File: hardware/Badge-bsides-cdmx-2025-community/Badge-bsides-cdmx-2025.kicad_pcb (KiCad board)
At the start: 2 copper layers, 49.9 x 109.8 mm, 51 parts, among them J1 SWDIO, J3 ADDON, J4 Conn_01x04_Pin, J5 I2C, J6 Conn_01x04_Pin, P6 USB_C_Plug_USB2.0, Q3 DMG3415U-7, SW10 SW_Push, SW11 ON, SW2 RESET, SW7 SW_Push, SW8 SW_Push, SW9 SW_Push, U1 PY32F030F28U6TR, U6 AP2112K-3.3

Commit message: feat(Hw):Update_BOM_And_Route
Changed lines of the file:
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@@
 				(font
 					(size 0.001 0.001)
+					(thickness 0.15)
 				)
 			)
@@
 				(font
 					(size 0.001 0.001)
+					(thickness 0.15)
 				)
 			)
@@
 				(font
 					(size 0.001 0.001)
+					(thickness 0.15)
 				)
 			)
@@
 				(font
 					(size 0.001 0.001)
+					(thickness 0.15)
 				)
 			)
@@
 				(font
 					(size 0.001 0.001)
+					(thickness 0.15)
 				)
 				(justify mirror)
@@
 				(font
 					(size 0.001 0.001)
+					(thickness 0.15)
 				)
 				(justify mirror)
@@
 				(font
 					(size 0.001 0.001)
+					(thickness 0.15)
 				)
 				(justify mirror)
@@
 				(font
 					(size 0.001 0.001)
+					(thickness 0.15)
 				)
 				(justify mirror)
@@
 				(font
 					(size 0.001 0.001)
+					(thickness 0.15)
 				)
 				(justify mirror)
@@
 				(font
 					(size 0.001 0.001)
+					(thickness 0.15)
 				)
 				(justify mirror)
@@
 				(font
 					(size 0.001 0.001)
+					(thickness 0.15)
 				)
 				(justify mirror)
@@
 				(font
 					(size 0.001 0.001)
+					(thickness 0.15)
 				)
 				(justify mirror)
@@
 				(font
 					(size 0.001 0.001)
+					(thickness 0.15)
 				)
 				(justify mirror)
@@
 				(font
 					(size 0.001 0.001)
+					(thickness 0.15)
 				)
 				(justify mirror)
@@
 				(font
 					(size 0.001 0.001)
+					(thickness 0.15)
 				)
 				(justify mirror)
@@
 				(font
 					(size 0.001 0.001)
+					(thickness 0.15)
 				)
 				(justify mirror)
@@
 	)
 	(segment
-		(start 64.281333 83.964333)
-		(end 61.731333 83.964333)
-		(width 0.3)
-		(layer "F.Cu")
-		(net 2)
-	)
-	(segment
-		(start 64.891333 79.654333)
-		(end 64.891333 83.354333)
+		(start 65.921333 64.844333)
+		(end 65.921333 79.314333)
 		(width 0.3)
 		(layer "F.Cu")
@@
 	)
 	(segment
-		(start 64.891333 83.354333)
-		(end 64.281333 83.964333)
+		(start 36.341333 49.754333)
+		(end 37.341333 50.754333)
 		(width 0.3)
 		(layer "F.Cu")
@@
 	)
 	(segment
-		(start 65.921333 64.844333)
-		(end 65.921333 79.314333)
+		(start 73.891333 58.334333)
+		(end 73.891333 62.694333)
 		(width 0.3)
 		(layer "F.Cu")
@@
 	)
 	(segment
-		(start 36.341333 49.754333)
-		(end 37.341333 50.754333)
+		(start 63.995 87.305)
+		(end 64.891333 86.408667)
 		(width 0.3)
 		(layer "F.Cu")
@@
 	)
 	(segment
-		(start 73.891333 58.334333)
-		(end 73.891333 62.694333)
+		(start 64.891333 86.408667)
+		(end 64.891333 79.654333)
 		(width 0.3)
 		(layer "F.Cu")
@@
 	)
 	(via
-		(at 61.731333 83.964333)
+		(at 63.995 87.305)
 		(size 0.6)
 		(drill 0.3)
@@
 	)
 	(segment
-		(start 61.65 84.045666)
-		(end 61.731333 83.964333)
-		(width 0.3)
-		(layer "B.Cu")
-		(net 2)
-	)
-	(segment
 		(start 43.76 50.754333)
 		(end 41.081333 50.754333)
@@
 	)
 	(segment
-		(start 61.35 88.22)
-		(end 61.65 87.92)
-		(width 0.3)
-		(layer "B.Cu")
-		(net 2)
-	)
-	(segment
 		(start 53.875 63.348)
 		(end 53.88 63.343)
@@
 	)
 	(segment
-		(start 61.65 87.92)
-		(end 61.65 84.045666)
+		(start 63.995 87.305)
+		(end 63.08 88.22)
 		(width 0.3)
 		(layer "B.Cu")
@@
 	)
 	(segment
+		(start 63.08 88.22)
+		(end 51.01 88.22)
+		(width 0.3)
+		(layer "B.Cu")
+		(net 2)
+	)
+	(segment
 		(start 51 88.22)
 		(end 51.01 88.22)
@@
 	)
 	(segment
-		(start 51.01 88.22)
-		(end 61.35 88.22)
-		(width 0.3)
-		(layer "B.Cu")
-		(net 2)
-	)
-	(segment
 		(start 43.76 50.754333)
 		(end 43.885666 50.754333)
@@
 	)
 	(segment
-		(start 46.94 65.42)
-		(end 45.6 64.08)
+		(start 45.6 33.85)
+		(end 45.21 33.46)
 		(width 0.2)
 		(layer "F.Cu")
@@
 	)
 	(segment
-		(start 51.962333 66.012333)
-		(end 51.37 65.42)
+		(start 46.94 65.42)
+		(end 45.6 64.08)
 		(width 0.2)
 		(layer "F.Cu")
@@
 	)
 	(segment
-		(start 51.962333 78.067667)
-		(end 51.962333 66.012333)
+		(start 51.96 78.07)
+		(end 51.962333 78.067667)
 		(width 0.2)
 		(layer "F.Cu")
@@
 	)
 	(segment
-		(start 51.96 78.07)
-		(end 51.962333 78.067667)
+		(start 45.6 64.08)
+		(end 45.6 33.85)
 		(width 0.2)
 		(layer "F.Cu")
@@
 	)
 	(segment
-		(start 45.6 33.56)
-		(end 45.5 33.46)
+		(start 45.21 33.46)
+		(end 42.93125 33.46)
 		(width 0.2)
 		(layer "F.Cu")
@@
 	)
 	(segment
-		(start 45.5 33.46)
-		(end 42.93125 33.46)
+		(start 51.962333 66.012333)
+		(end 51.37 65.42)
 		(width 0.2)
 		(layer "F.Cu")
@@
 	)
 	(segment
-		(start 45.6 64.08)
-		(end 45.6 33.56)
+		(start 51.962333 78.067667)
+		(end 51.962333 66.012333)
 		(width 0.2)
 		(layer "F.Cu")
@@
 	)
 	(segment
-		(start 81.59 109.73569)
-		(end 81.59 108.853)
-		(width 0.5)
-		(layer "B.Cu")
-		(net 26)
-	)
-	(segment
 		(start 82.014848 112.489502)
-		(end 82.014848 110.160538)
+		(end 82.014848 109.277848)
 		(width 0.5)
 		(layer "B.Cu")
@@
 	)
 	(segment
-		(start 44.25 107.344333)
-		(end 43.04 106.134333)
-		(width 0.5)
-		(layer "B.Cu")
-		(net 26)
-	)
-	(segment
-		(start 82.014848 110.160538)
-		(end 81.59 109.73569)
+		(start 82.014848 109.277848)
+		(end 80.081333 107.344333)
 		(width 0.5)
 		(layer "B.Cu")
@@
 	)
 	(segment
-		(start 81.59 108.853)
-		(end 80.081333 107.344333)
+		(start 44.25 107.344333)
+		(end 43.04 106.134333)
 		(width 0.5)
 		(layer "B.Cu")

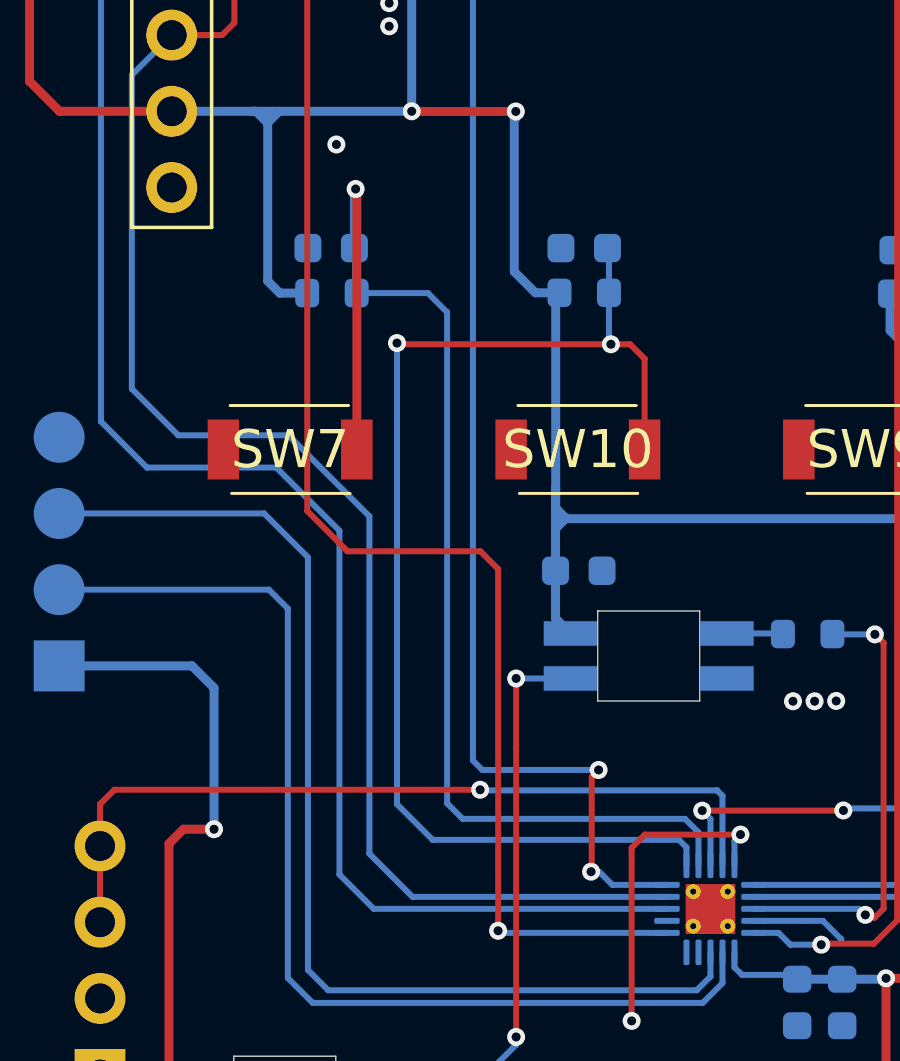
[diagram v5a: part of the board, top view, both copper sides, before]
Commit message: feat(Hw):BoM_Updated_Staff_Community
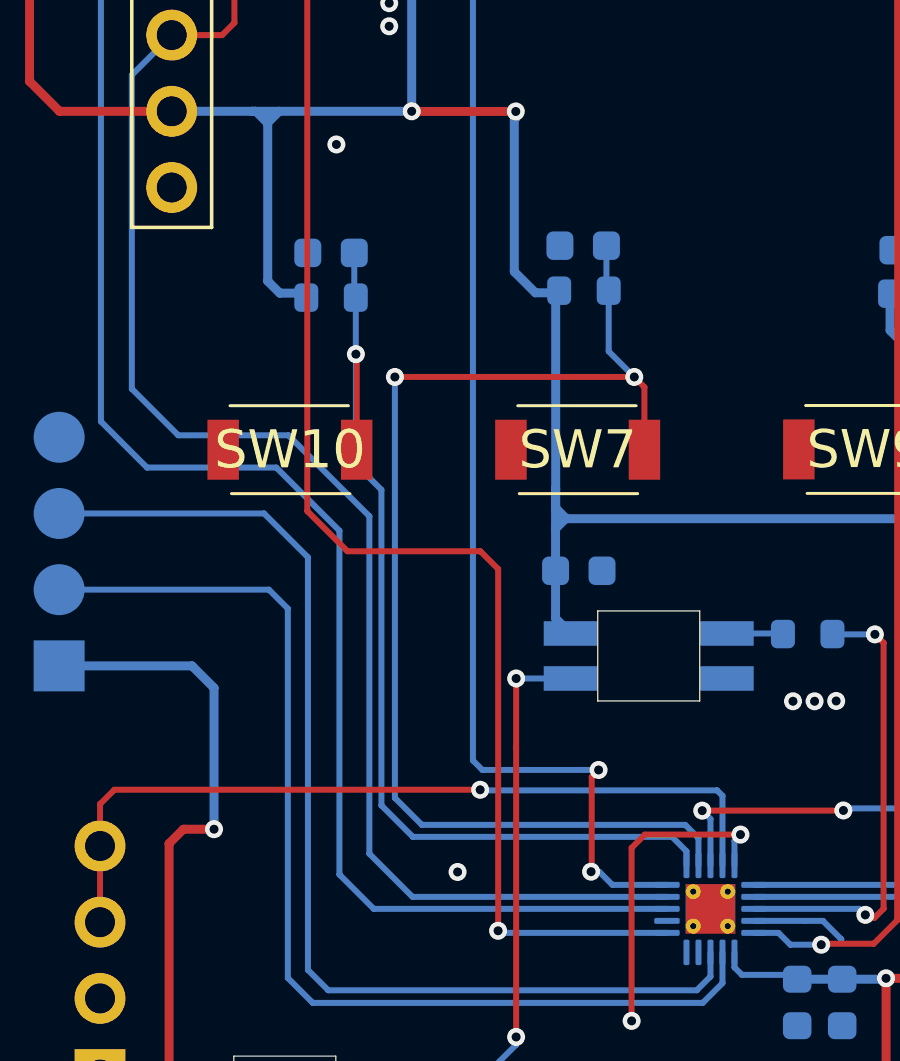
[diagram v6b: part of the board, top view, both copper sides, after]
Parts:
- moved SW10 9.60 mm to (45.0, 62.0)
- moved SW7 9.59 mm to (54.6, 62.0)
- moved C70 8.44 mm to (46.4, 55.5)
- moved R8 8.44 mm to (46.4, 57.0)
- moved R7 8.40 mm to (54.8, 56.7)
- moved C69 8.40 mm to (54.8, 55.2)
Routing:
- net /BTTN4: track 41.0 -> 33.3 mm, vias 2 -> 1
- net /BTTN3: track 41.7 -> 40.9 mm, vias 1 -> 2
- net GND: vias 7 -> 8
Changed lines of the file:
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@@
 	(footprint "Footprints:TS1088R02026"
 		(layer "F.Cu")
-		(at 54.618 62.026595)
+		(at 45.022 62.033405)
 		(descr "TS-1088R-02026-1")
 		(tags "Switch")
@@
 	(footprint "Footprints:TS1088R02026"
 		(layer "F.Cu")
-		(at 45.026333 62.026595)
+		(at 54.613667 62.033405)
 		(descr "TS-1088R-02026-1")
 		(tags "Switch")
@@
 	(footprint "Capacitor_SMD:C_0603_1608Metric"
 		(layer "B.Cu")
-		(at 46.396333 55.314333 180)
+		(at 54.796333 55.234333 180)
 		(descr "Capacitor SMD 0603 (1608 Metric), square (rectangular) end terminal, IPC-7351 nominal, (Body size source: IPC-SM-782 page 76, https://www.pcb-3d.com/wordpress/wp-content/uploads/ipc-sm-782a_amendment_1_and_2.pdf), generated with kicad-footprint-generator")
 		(tags "capacitor")
@@
 	(footprint "Resistor_SMD:R_0603_1608Metric"
 		(layer "B.Cu")
-		(at 46.421333 56.814333 180)
+		(at 54.821333 56.734333 180)
 		(descr "Resistor SMD 0603 (1608 Metric), square (rectangular) end terminal, IPC-7351 nominal, (Body size source: IPC-SM-782 page 72, https://www.pcb-3d.com/wordpress/wp-content/uploads/ipc-sm-782a_amendment_1_and_2.pdf), generated with kicad-footprint-generator")
 		(tags "resistor")
@@
 	(footprint "Resistor_SMD:R_0603_1608Metric"
 		(layer "B.Cu")
-		(at 54.831333 56.804333 180)
+		(at 46.391333 56.964333 180)
 		(descr "Resistor SMD 0603 (1608 Metric), square (rectangular) end terminal, IPC-7351 nominal, (Body size source: IPC-SM-782 page 72, https://www.pcb-3d.com/wordpress/wp-content/uploads/ipc-sm-782a_amendment_1_and_2.pdf), generated with kicad-footprint-generator")
 		(tags "resistor")
@@
 	(footprint "Capacitor_SMD:C_0603_1608Metric"
 		(layer "B.Cu")
-		(at 54.831333 55.314333 180)
+		(at 46.391333 55.474333 180)
 		(descr "Capacitor SMD 0603 (1608 Metric), square (rectangular) end terminal, IPC-7351 nominal, (Body size source: IPC-SM-782 page 76, https://www.pcb-3d.com/wordpress/wp-content/uploads/ipc-sm-782a_amendment_1_and_2.pdf), generated with kicad-footprint-generator")
 		(tags "capacitor")
@@
 	)
 	(via
+		(at 50.61 76.11)
+		(size 0.6)
+		(drill 0.3)
+		(layers "F.Cu" "B.Cu")
+		(free yes)
+		(net 1)
+	)
+	(via
 		(at 46.57 51.86)
 		(size 0.6)
@@
 	)
 	(segment
-		(start 47.211333 53.344333)
-		(end 47.251333 53.384333)
-		(width 0.3)
+		(start 56.838667 59.948667)
+		(end 56.838667 62.033405)
+		(width 0.2)
 		(layer "F.Cu")
 		(net 31)
 	)
 	(segment
-		(start 47.251333 53.384333)
-		(end 47.251333 62.026595)
-		(width 0.3)
+		(start 56.5 59.61)
+		(end 48.52 59.61)
+		(width 0.2)
+		(layer "F.Cu")
+		(net 31)
+	)
+	(segment
+		(start 56.5 59.61)
+		(end 56.838667 59.948667)
+		(width 0.2)
 		(layer "F.Cu")
 		(net 31)
 	)
 	(via
-		(at 47.211333 53.344333)
+		(at 56.5 59.61)
 		(size 0.6)
 		(drill 0.3)
@@
 		(net 31)
 	)
-	(segment
-		(start 58.64 75.89)
-		(end 58.64 74.79)
-		(width 0.2)
-		(layer "B.Cu")
+	(via
+		(at 48.52 59.61)
+		(size 0.6)
+		(drill 0.3)
+		(layers "F.Cu" "B.Cu")
 		(net 31)
 	)
 	(segment
-		(start 58.19 74.34)
-		(end 50.78 74.34)
+		(start 55.571333 55.234333)
+		(end 55.571333 56.659333)
 		(width 0.2)
 		(layer "B.Cu")
@@
 	)
 	(segment
-		(start 47.246333 55.389333)
-		(end 47.171333 55.314333)
-		(width 0.3)
-		(layer "B.Cu")
-		(net 31)
-	)
-	(segment
-		(start 50.261333 73.821333)
-		(end 50.261333 57.454333)
+		(start 58.64 75.89)
+		(end 58.64 74.98)
 		(width 0.2)
 		(layer "B.Cu")
@@
 	)
 	(segment
-		(start 47.246333 56.814333)
-		(end 47.246333 55.389333)
-		(width 0.3)
+		(start 58.64 74.98)
+		(end 58.2 74.54)
+		(width 0.2)
 		(layer "B.Cu")
 		(net 31)
 	)
 	(segment
-		(start 50.261333 57.454333)
-		(end 49.621333 56.814333)
+		(start 58.2 74.54)
+		(end 49.42 74.54)
 		(width 0.2)
 		(layer "B.Cu")
@@
 	)
 	(segment
-		(start 50.78 74.34)
-		(end 50.261333 73.821333)
+		(start 49.42 74.54)
+		(end 48.52 73.64)
 		(width 0.2)
 		(layer "B.Cu")
@@
 	)
 	(segment
-		(start 49.621333 56.814333)
-		(end 47.246333 56.814333)
+		(start 48.52 73.64)
+		(end 48.52 59.61)
 		(width 0.2)
 		(layer "B.Cu")
@@
 	)
 	(segment
-		(start 47.171333 53.384333)
-		(end 47.211333 53.344333)
-		(width 0.3)
+		(start 55.646333 56.734333)
+		(end 55.646333 58.756333)
+		(width 0.2)
 		(layer "B.Cu")
 		(net 31)
 	)
 	(segment
-		(start 47.171333 55.314333)
-		(end 47.171333 53.384333)
-		(width 0.3)
+		(start 55.646333 58.756333)
+		(end 56.5 59.61)
+		(width 0.2)
 		(layer "B.Cu")
 		(net 31)
 	)
 	(segment
-		(start 58.64 74.79)
-		(end 58.19 74.34)
+		(start 55.571333 56.659333)
+		(end 55.646333 56.734333)
 		(width 0.2)
 		(layer "B.Cu")
@@
 	)
 	(segment
-		(start 48.59 58.48)
-		(end 48.63 58.52)
+		(start 47.247 58.877)
+		(end 47.247 62.033405)
 		(width 0.2)
 		(layer "F.Cu")
@@
 	)
 	(segment
-		(start 48.63 58.52)
-		(end 55.72 58.52)
-		(width 0.2)
-		(layer "F.Cu")
-		(net 32)
-	)
-	(segment
-		(start 56.843 59.003)
-		(end 56.36 58.52)
-		(width 0.2)
-		(layer "F.Cu")
-		(net 32)
-	)
-	(segment
-		(start 56.36 58.52)
-		(end 55.72 58.52)
-		(width 0.2)
-		(layer "F.Cu")
-		(net 32)
-	)
-	(segment
-		(start 56.843 62.026595)
-		(end 56.843 59.003)
+		(start 47.22 58.85)
+		(end 47.247 58.877)
 		(width 0.2)
 		(layer "F.Cu")
@@
 	)
 	(via
-		(at 55.72 58.52)
+		(at 47.22 58.85)
 		(size 0.6)
 		(drill 0.3)
@@
 		(net 32)
 	)
-	(via
-		(at 48.59 58.48)
-		(size 0.6)
-		(drill 0.3)
-		(layers "F.Cu" "B.Cu")
+	(segment
+		(start 48.071333 73.891333)
+		(end 48.071333 63.371333)
+		(width 0.2)
+		(layer "B.Cu")
 		(net 32)
 	)
 	(segment
-		(start 55.656333 58.456333)
-		(end 55.656333 56.804333)
+		(start 47.22 62.52)
+		(end 47.22 58.85)
 		(width 0.2)
 		(layer "B.Cu")
@@
 	)
 	(segment
-		(start 55.58 55.340666)
-		(end 55.606333 55.314333)
+		(start 47.216333 56.964333)
+		(end 47.216333 58.846333)
 		(width 0.2)
 		(layer "B.Cu")
@@
 	)
 	(segment
-		(start 55.656333 55.364333)
-		(end 55.606333 55.314333)
+		(start 47.216333 58.846333)
+		(end 47.22 58.85)
 		(width 0.2)
 		(layer "B.Cu")
@@
 	)
 	(segment
-		(start 48.59 58.48)
-		(end 48.59 73.85)
+		(start 57.76 74.94)
+		(end 49.12 74.94)
 		(width 0.2)
 		(layer "B.Cu")
@@
 	)
 	(segment
-		(start 55.656333 56.804333)
-		(end 55.656333 55.364333)
+		(start 49.12 74.94)
+		(end 48.071333 73.891333)
 		(width 0.2)
 		(layer "B.Cu")
@@
 	)
 	(segment
-		(start 55.72 58.52)
-		(end 55.656333 58.456333)
+		(start 47.166333 56.914333)
+		(end 47.216333 56.964333)
 		(width 0.2)
 		(layer "B.Cu")
@@
 	)
 	(segment
-		(start 57.99 75.04)
-		(end 58.24 75.29)
+		(start 48.071333 63.371333)
+		(end 47.22 62.52)
 		(width 0.2)
 		(layer "B.Cu")
@@
 	)
 	(segment
-		(start 58.24 75.29)
-		(end 58.24 75.89)
+		(start 47.166333 55.474333)
+		(end 47.166333 56.914333)
 		(width 0.2)
 		(layer "B.Cu")
@@
 	)
 	(segment
-		(start 48.59 73.85)
-		(end 49.78 75.04)
+		(start 58.24 75.42)
+		(end 57.76 74.94)
 		(width 0.2)
 		(layer "B.Cu")
@@
 	)
 	(segment
-		(start 49.78 75.04)
-		(end 57.99 75.04)
+		(start 58.24 75.89)
+		(end 58.24 75.42)
 		(width 0.2)
 		(layer "B.Cu")

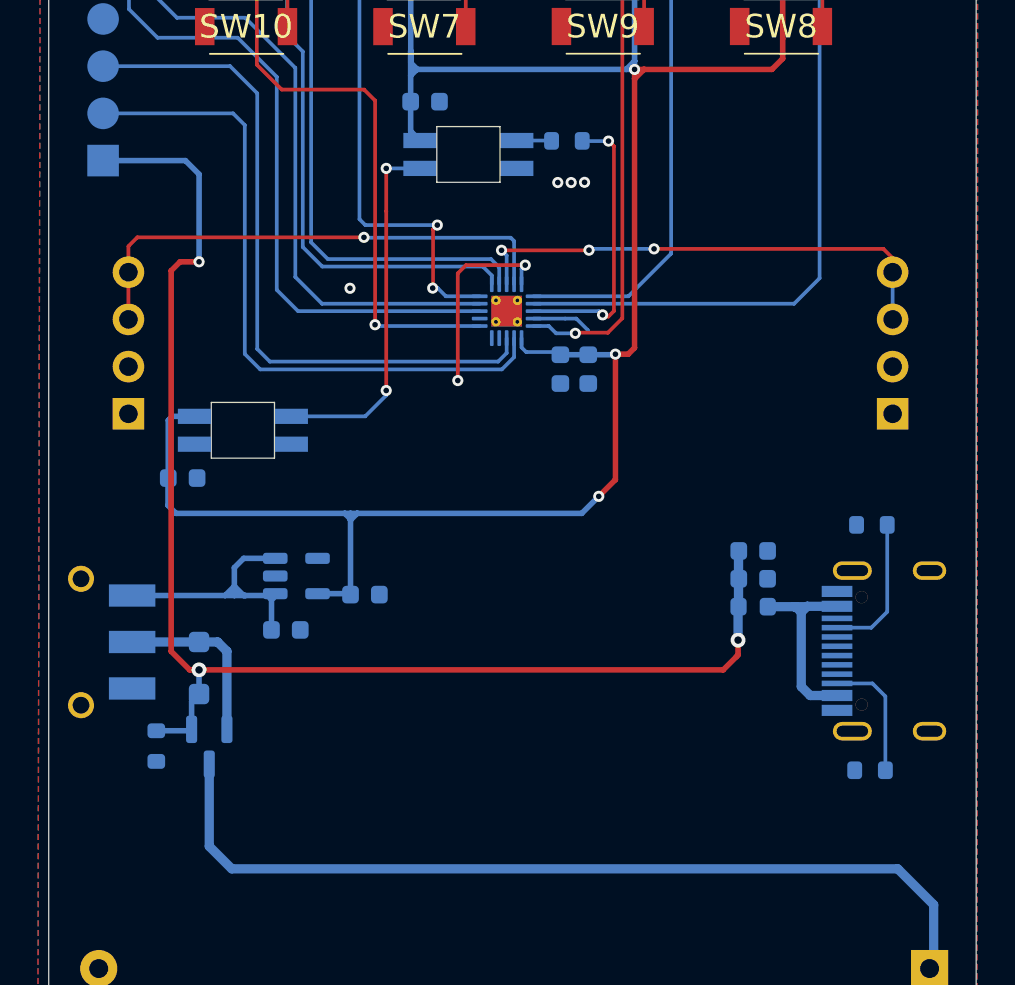
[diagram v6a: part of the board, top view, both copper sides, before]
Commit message: feat(Hw)USB_C_Deleted
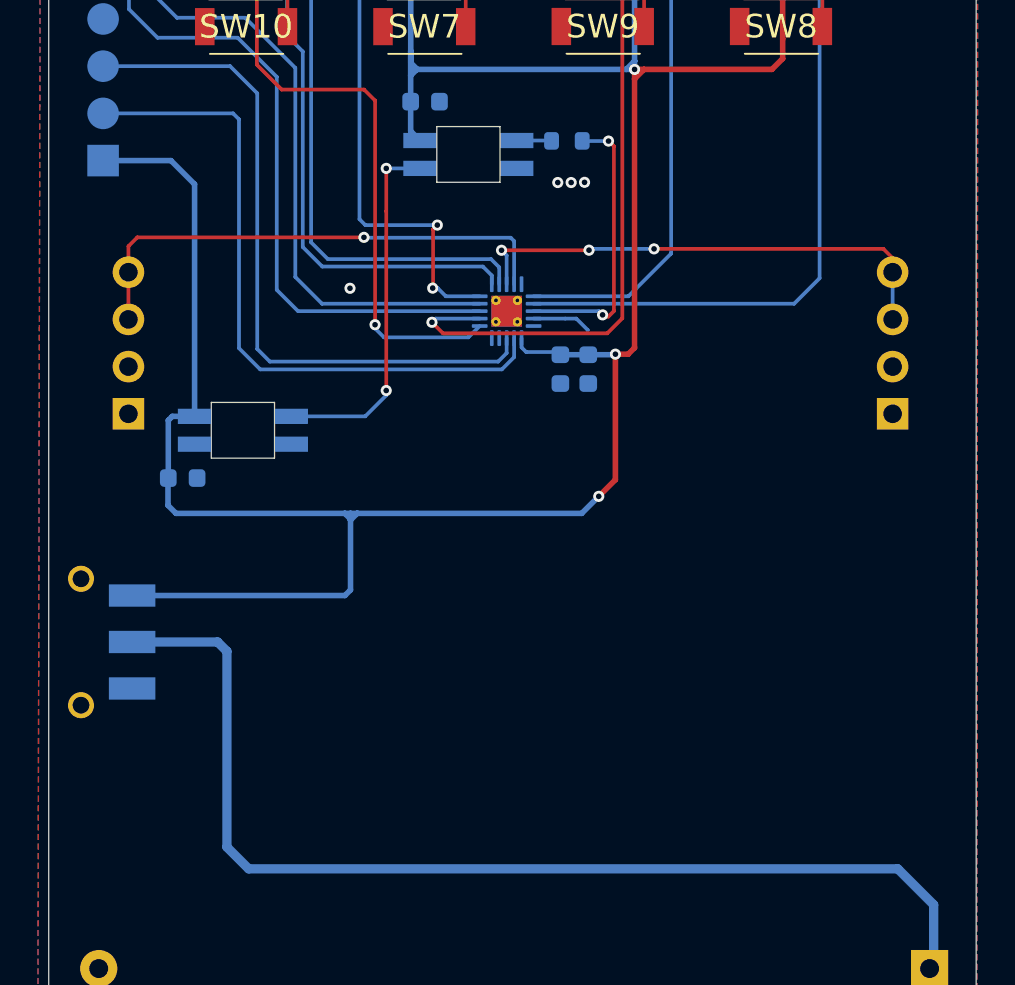
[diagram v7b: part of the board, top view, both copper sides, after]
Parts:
- removed C10, C26, C27: 10uF, Capacitor_SMD:C_0603_1608Metric
- removed C33: 100nF, Capacitor_SMD:C_0603_1608Metric
- removed D4: MBR120, Diode_SMD:D_SOD-123F
- removed F3: 750mA, Fuse:Fuse_0603_1608Metric
- removed P6: USB_C_Plug_USB2.0, Footprints:C393939
- removed Q3: DMG3415U-7, Package_TO_SOT_SMD:SOT-23
- removed R10: 100K, Resistor_SMD:R_0603_1608Metric
- removed R41, R45: 5k1, Resistor_SMD:R_0603_1608Metric
- removed U6: AP2112K-3.3, Package_TO_SOT_SMD:SOT-23-5
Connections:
- J1 pad 1: VBUS -> +3.3V
- SW11 pad 2: Net-(D4-K) -> +BATT
- SW11 pad 3: Net-(SW11-A) -> +3.3V
- U1 pad 12: unconnected-(U1-PF4/BOOT0-Pad12) -> /GPIO2
- U1 pad 5: /GPIO2 -> unconnected-(U1-PA12-Pad5)
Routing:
- net VBUS: track 74.5 -> 0.00 mm, vias 3 -> 0
- net +3.3V: track 201.5 -> 229.2 mm
- net Net-(SW11-A): track 15.2 -> 0.00 mm
- net Net-(F3-Pad1): track 10.8 -> 0.00 mm
- net /LED2: track 10.7 -> 0.00 mm, vias 2 -> 0
- net +BATT: track 48.2 -> 58.7 mm
- net Net-(D4-K): track 9.51 -> 0.00 mm
- net /GPIO2: track 76.4 -> 84.6 mm
- net Net-(P6-CC): track 7.73 -> 0.00 mm
- net Net-(P6-VCONN): track 6.86 -> 0.00 mm
- net /GPIO1: track 57.9 -> 58.6 mm
